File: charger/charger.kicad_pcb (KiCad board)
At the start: 2 copper layers, 101.6 x 53.3 mm, 43 parts, among them J1 Barrel_Jack, P1 Digital, P10 CONN_01X01, P11 CONN_01X01, P12 CONN_01X01, P13 CONN_01X01, P2 Power, P3 Analog, P4 Analog, P5 PWM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

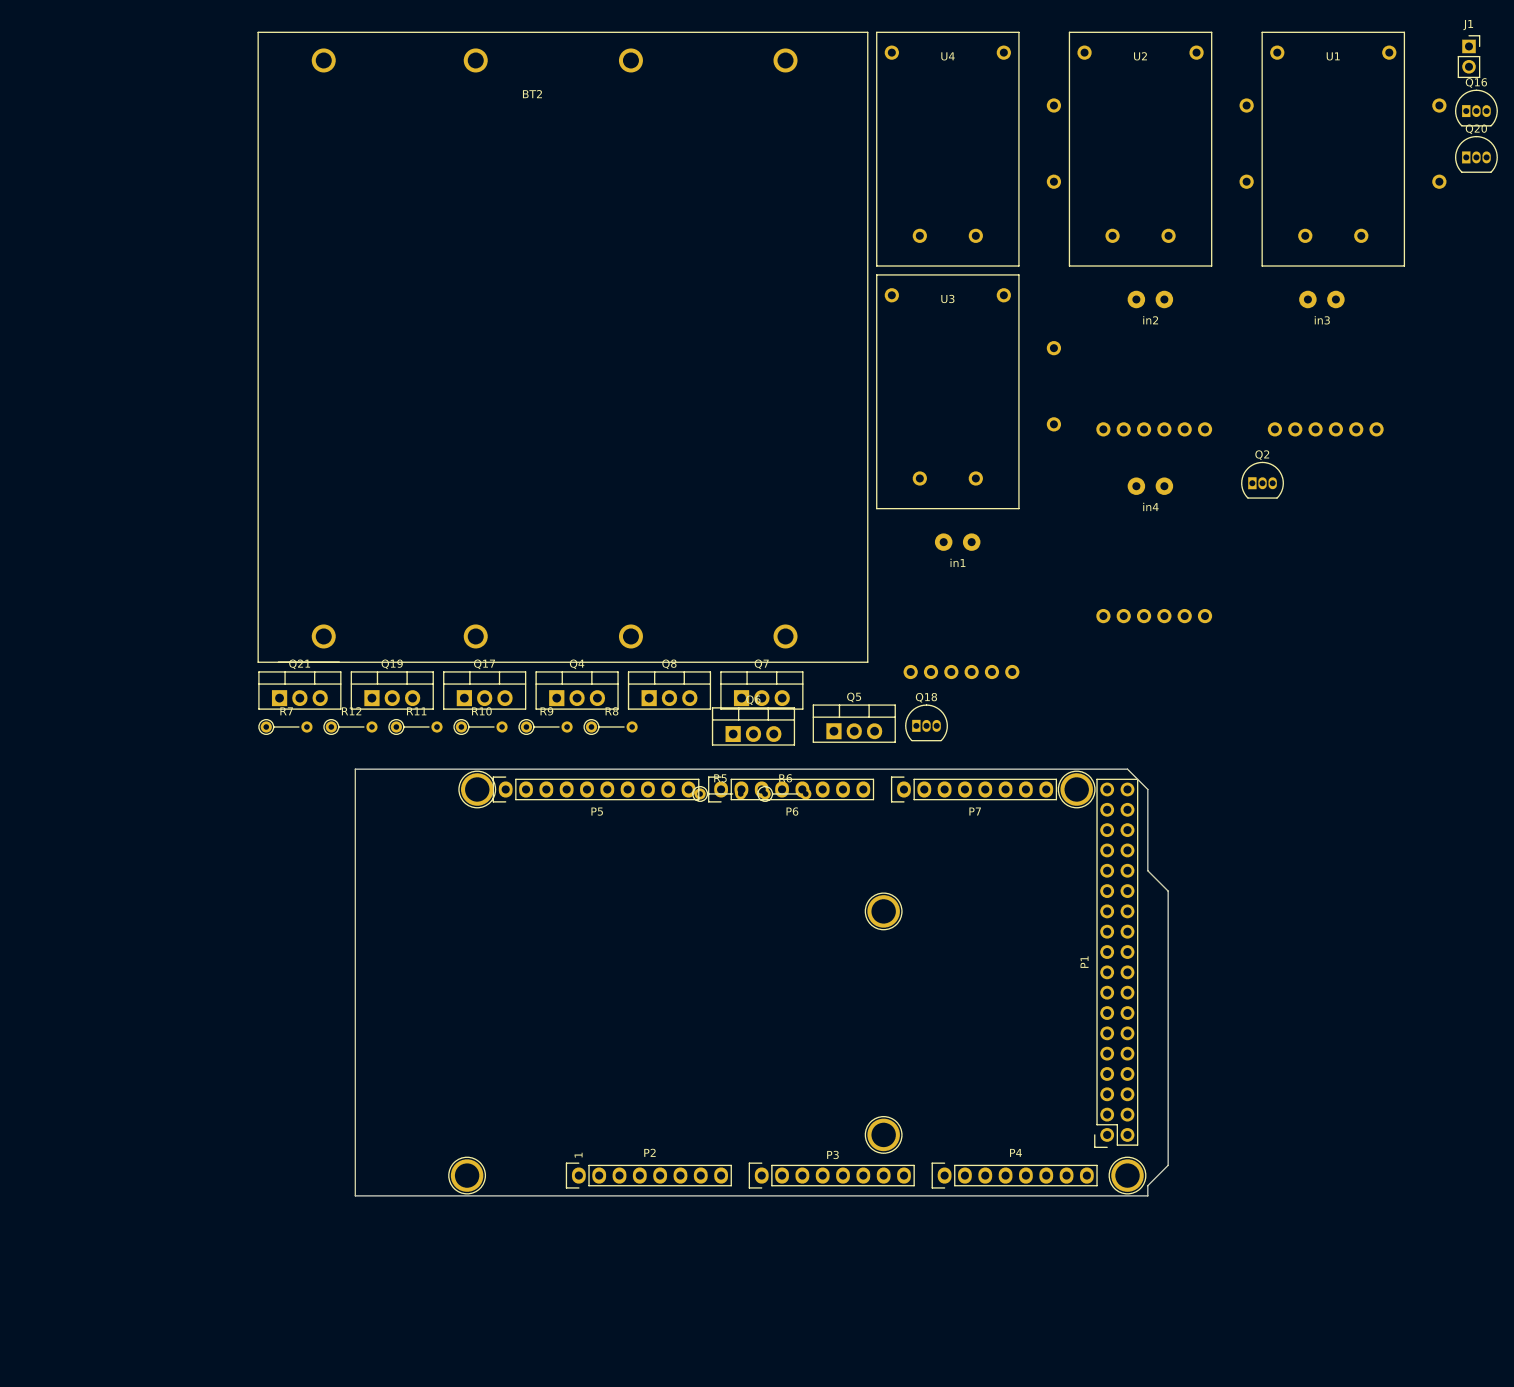
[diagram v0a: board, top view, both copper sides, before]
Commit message: adding 2 layer layout, circuit design for 1 and 2 layer
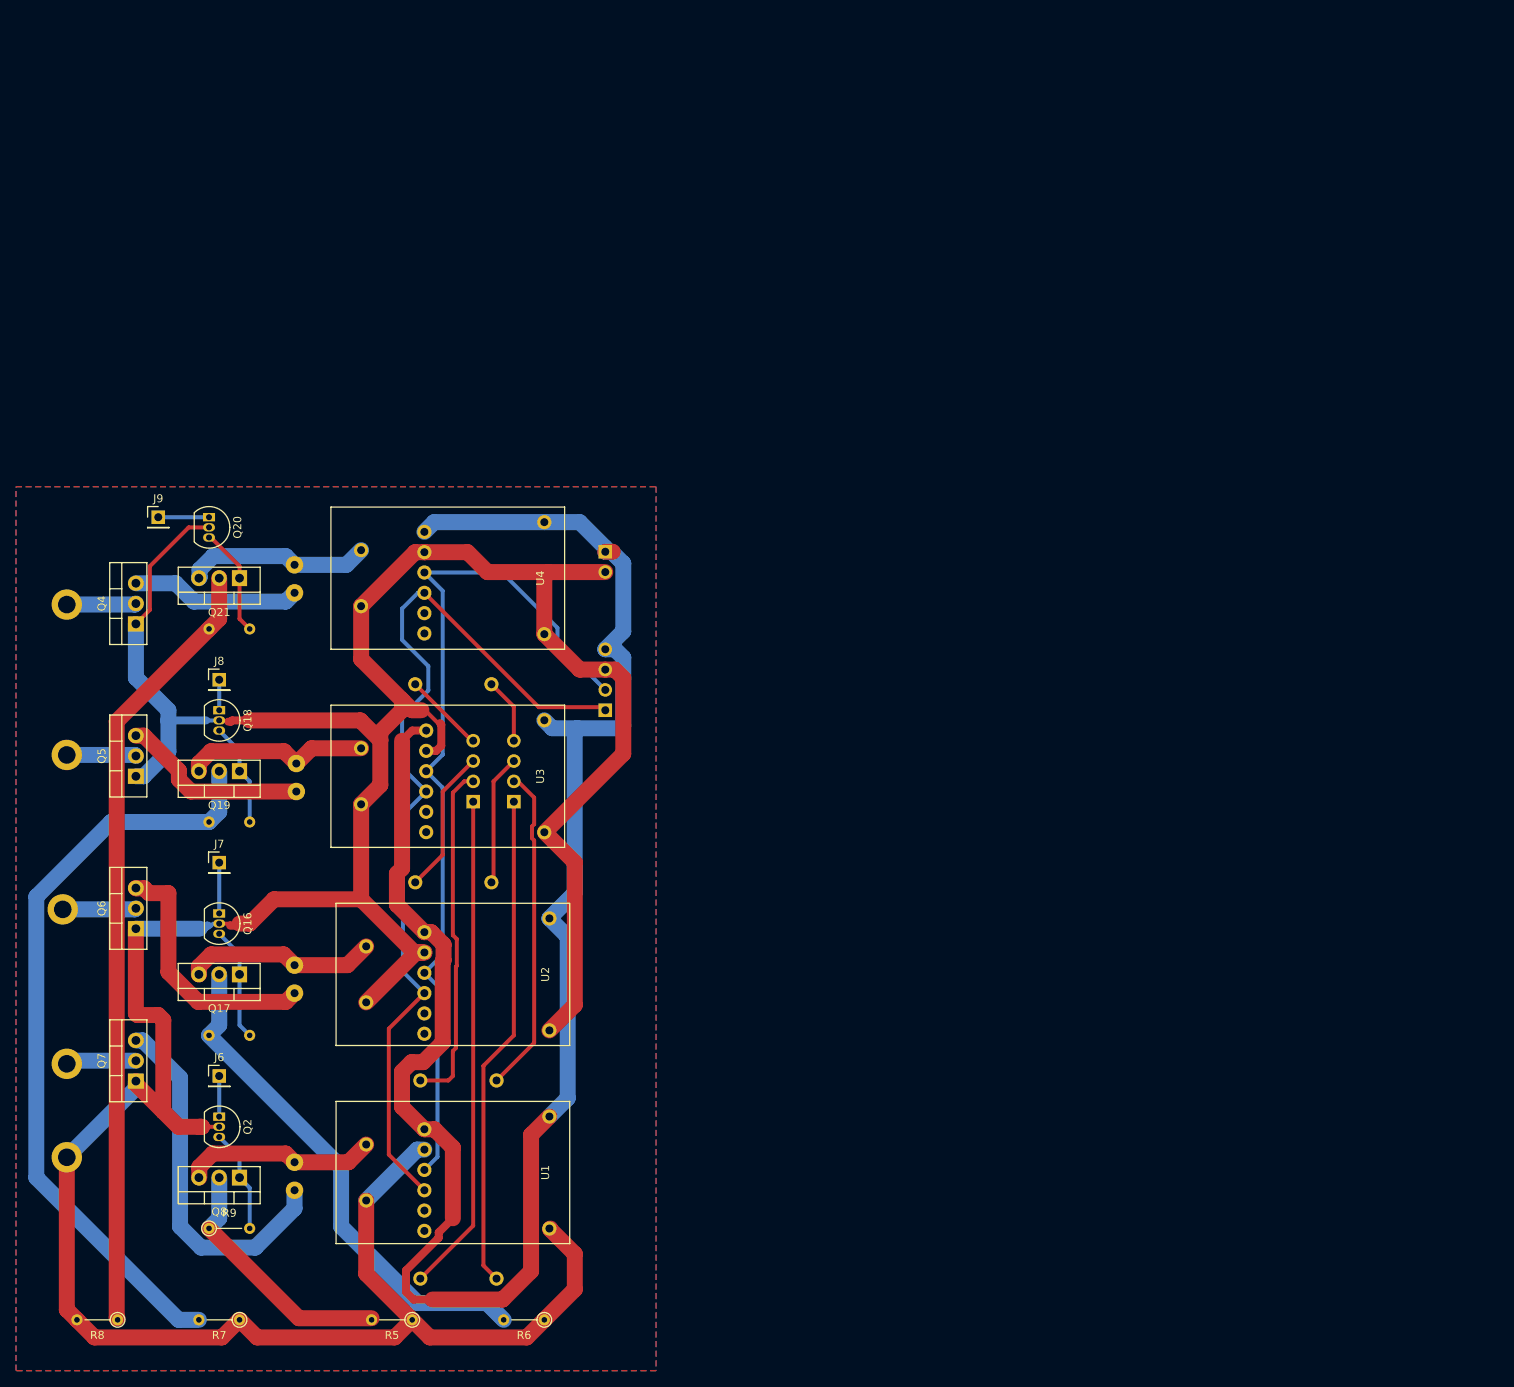
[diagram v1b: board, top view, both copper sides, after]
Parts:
- removed BT2: cellholder_4_18650, charger:battery_holder
- removed P1: Digital, Socket_Arduino_Mega:Socket_Strip_Arduino_2x18
- removed P10, P11, P12, P13, P8, P9: CONN_01X01, Socket_Arduino_Mega:Arduino_1pin
- removed P2: Power, Socket_Arduino_Mega:Socket_Strip_Arduino_1x08
- removed P3, P4: Analog, Socket_Arduino_Mega:Socket_Strip_Arduino_1x08
- removed P5: PWM, Socket_Arduino_Mega:Socket_Strip_Arduino_1x10
- removed P6: PWM, Socket_Arduino_Mega:Socket_Strip_Arduino_1x08
- removed P7: Communication, Socket_Arduino_Mega:Socket_Strip_Arduino_1x08
- added B1: Screw_Terminal_01x01, MountingHole:MountingHole_2.2mm_M2_DIN965_Pad, B.Cu at (67.3, 47.8)
- added B2: Screw_Terminal_01x01, MountingHole:MountingHole_2.2mm_M2_DIN965_Pad, B.Cu at (67.3, 66.5)
- added B3: Screw_Terminal_01x01, MountingHole:MountingHole_2.2mm_M2_DIN965_Pad, B.Cu at (66.8, 85.9)
- added B4: Screw_Terminal_01x01, MountingHole:MountingHole_2.2mm_M2_DIN965_Pad, B.Cu at (67.3, 105.2)
- added BGND1: Screw_Terminal_01x01, MountingHole:MountingHole_2.2mm_M2_DIN965_Pad, B.Cu at (67.3, 116.8)
- added J2: Conn_01x04, Connector_PinHeader_2.54mm:PinHeader_1x04_P2.54mm_Vertical, B.Cu at (123.2, 72.4)
- added J3: Conn_01x04, Connector_PinHeader_2.54mm:PinHeader_1x04_P2.54mm_Vertical, B.Cu at (134.6, 61.0)
- added J4: Conn_01x04, Connector_PinHeader_2.54mm:PinHeader_1x04_P2.54mm_Vertical, B.Cu at (118.1, 72.4)
- added J6: Conn_01x01, Connector_PinHeader_2.54mm:PinHeader_1x01_P2.54mm_Vertical, F.Cu at (86.4, 106.7)
- added J7: Conn_01x01, Connector_PinHeader_2.54mm:PinHeader_1x01_P2.54mm_Vertical, F.Cu at (86.4, 80.0)
- added J8: Conn_01x01, Connector_PinHeader_2.54mm:PinHeader_1x01_P2.54mm_Vertical, F.Cu at (86.4, 57.1)
- added J9: Conn_01x01, Connector_PinHeader_2.54mm:PinHeader_1x01_P2.54mm_Vertical, F.Cu at (78.7, 36.8)
- J1, R10, R11, R12, in1, in2, in3, in4: moved to B.Cu
- moved Q16 185.4 mm to (86.4, 86.4), turned to 270 degrees
- moved U1 170.9 mm to (127.6, 118.7), turned to 270 degrees
- moved Q20 163.5 mm to (85.1, 36.8), turned to 270 degrees
- moved Q2 151.5 mm to (86.4, 111.8), turned to 270 degrees
- moved U2 136.9 mm to (127.6, 94.0), turned to 270 degrees
- moved J1 125.1 mm to (134.6, 41.1), turned to 180 degrees
- moved in3 121.3 mm to (106.9, 65.0), turned to 270 degrees
- moved in2 115.1 mm to (106.7, 90.2), turned to 270 degrees
- moved R8 94.9 mm to (73.7, 137.2), turned to 180 degrees
- moved in1 93.1 mm to (106.7, 114.8), turned to 270 degrees
- moved in4 91.8 mm to (106.7, 40.1), turned to 270 degrees
- moved Q7 89.6 mm to (75.9, 107.3), turned to 90 degrees
- moved Q5 87.4 mm to (75.9, 69.2), turned to 90 degrees
- moved Q18 87.2 mm to (86.4, 61.0), turned to 270 degrees
- moved U4 82.8 mm to (127.0, 44.5), turned to 270 degrees
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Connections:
- Q16 pad 1: /23 -> /25
- Q18 pad 1: /24 -> /27
- Q2 pad 1: /22 -> /23
- Q20 pad 1: /25 -> /29
- U2 pad 5: /41 -> /42
- U3 pad 5: /42 -> /44
- U4 pad 5: /43 -> /46
- in3 pad 3: (no net) -> VCC
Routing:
- net GND: track 0.00 -> 458.6 mm
- net VCC: track 0.00 -> 236.1 mm
- net /SDA: track 0.00 -> 115.0 mm
- net /SCL: track 0.00 -> 109.4 mm
- net Net-(Q21-Pad2): track 0.00 -> 97.9 mm
- net Net-(Q19-Pad2): track 0.00 -> 95.1 mm
- net Net-(Q17-Pad2): track 0.00 -> 64.0 mm
- net /A0: track 0.00 -> 62.4 mm
- net /40: track 0.00 -> 61.9 mm
- net Net-(Q7-Pad3): track 0.00 -> 45.8 mm
- net /A1: track 0.00 -> 43.2 mm
- net /42: track 0.00 -> 40.9 mm
- net Net-(Q6-Pad3): track 0.00 -> 32.0 mm
- net Net-(Q8-Pad2): track 0.00 -> 31.8 mm
- net /ina1Drain: track 0.00 -> 24.3 mm
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- added copper zone on F.Cu, net GND
- added copper zone on B.Cu, net VCC
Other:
- board outline removed
- net class Default: clearance 0.2 -> 0.4; trace_width 0.25 -> 0.5
- net class track-width added: clearance 0.25, trace_width 0.25, via_dia 0.6, via_drill 0.4
- rule trace_clearance: 0.2 -> 0.4
- board text removed: "1"
